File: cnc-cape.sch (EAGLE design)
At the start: 120 parts, among them IC1 LM2576hvt, IC2 74HC14N, IC3 74HC14N, IC4 74HCT244N, IC5 74HCT244N, IC6 74HC14N, IC7 LM1458N, J1 22-27-2041-04, J10 22-27-2031-03, J11 22-27-2031-03, J12 22-27-2031-03, J13 22-27-2031-03, J14 22-27-2031-03, J15 22-27-2031-03, J16 22-27-2031-03, J17 22-27-2031-03, J18 22-27-2031-03, J19 22-27-2031-03, J2 22-27-2041-04, J20 22-27-2031-03, J21 22-27-2031-03, J22 22-27-2031-03, J3 22-27-2041-04, J4 22-27-2041-04, J5 22-27-2041-04, J6 22-27-2031-03, J7 22-27-2031-03, J8 22-27-2031-03, J9 22-27-2031-03, K1 G2R2, K2 G2R2, K3 G2R2, Q1 2N7000, Q2 2N7000, T1 1n2222, T2 1n2222, T3 1n2222, X5 Power In

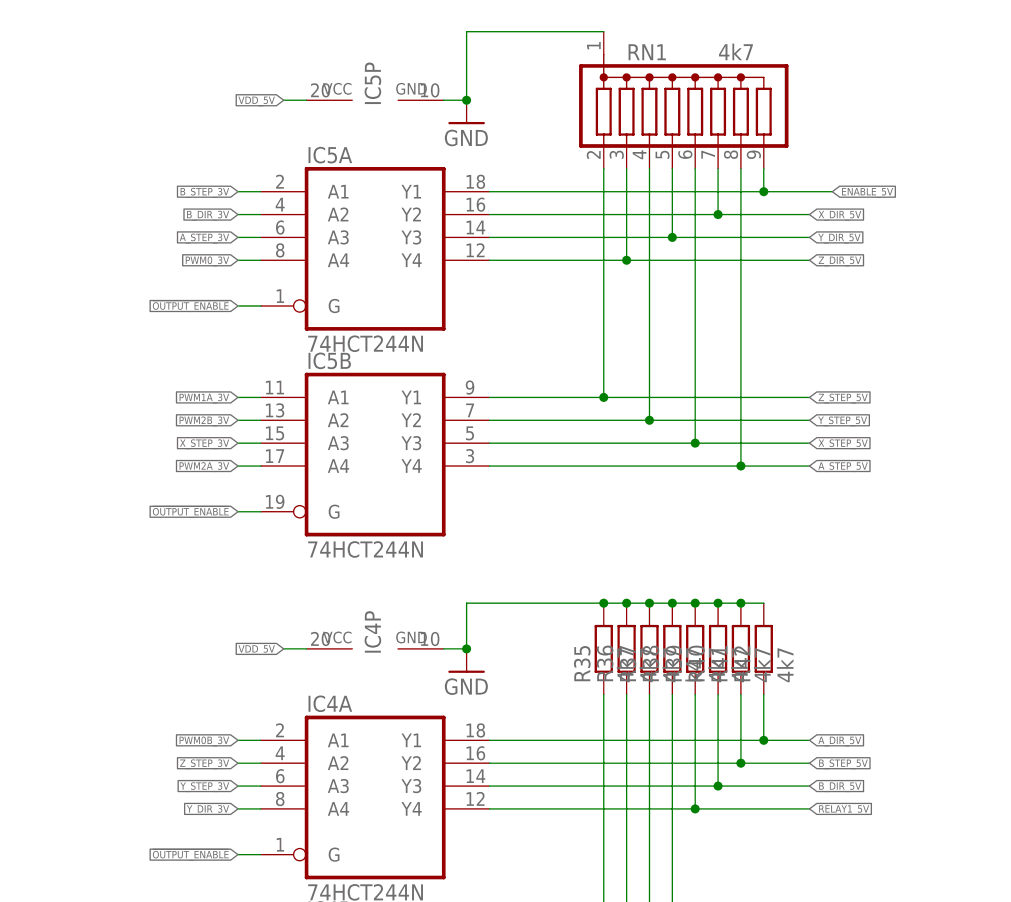
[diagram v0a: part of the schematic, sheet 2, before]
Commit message: Rearraged layout to reduce via count
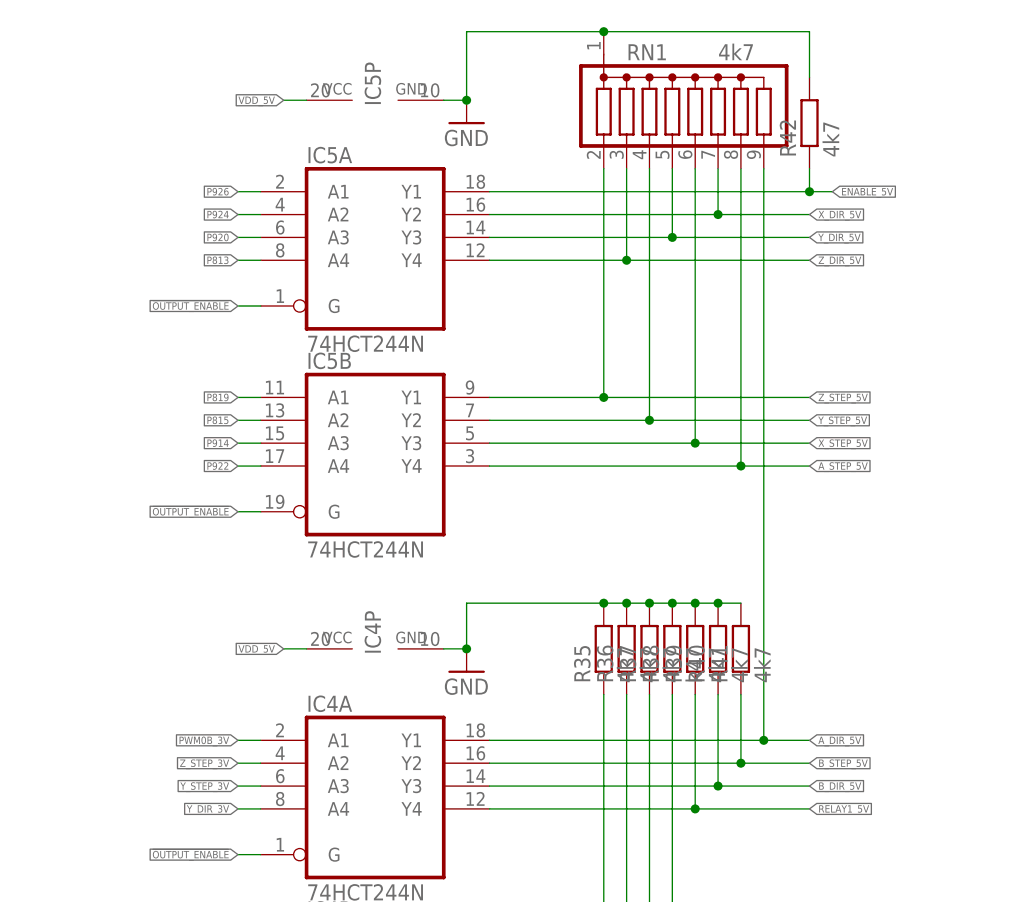
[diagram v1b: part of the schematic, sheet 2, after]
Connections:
- net B_DIR_3V renamed P924
- net B_STEP_3V renamed P926
- removed net A_STEP_3V: IC5A.A3, U$1.UART2_RXD
- removed net PWM0_3V: IC5A.A4, U$1.I2C2_SDA
- removed net PWM1A_3V: IC5B.A1, U$1.EHRPWM1A
- removed net PWM2A_3V: IC5B.A4, U$1.EHRPWM2A
- removed net PWM2B_3V: IC5B.A2, U$1.EHRPWM2B
- removed net X_STEP_3V: IC5B.A3, U$1.GPIO1_15
- new net P813: IC5A.A4, U$1.EHRPWM2B
- new net P815: IC5B.A2, U$1.GPIO1_15
- new net P819: IC5B.A1, U$1.EHRPWM2A
- new net P914: IC5B.A3, U$1.EHRPWM1A
- new net P920: IC5A.A3, U$1.I2C2_SDA
- new net P922: IC5B.A4, U$1.UART2_RXD
- net A_DIR_5V: now also RN1.9; no longer R42.1
- net ENABLE_5V: now also R42.1; no longer RN1.9
- net ENCODER0_A: now also IC2B.I, J7-2.S, LED2.C; no longer IC2C.I, J6-2.S, LED1.C
- net ENCODER0_B: now also IC2A.I, J8-2.S, LED3.C; no longer IC2B.I, J7-2.S, LED2.C
- net ENCODER0_I: now also IC2C.I, J6-2.S, LED1.C; no longer IC2A.I, J8-2.S, LED3.C
- net EQEP0A: now also IC2B.O; no longer IC2C.O
- net EQEP0B: now also IC2A.O; no longer IC2B.O
- net EQEP0I: now also IC2C.O; no longer IC2A.O
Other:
- moved on the sheet: R42

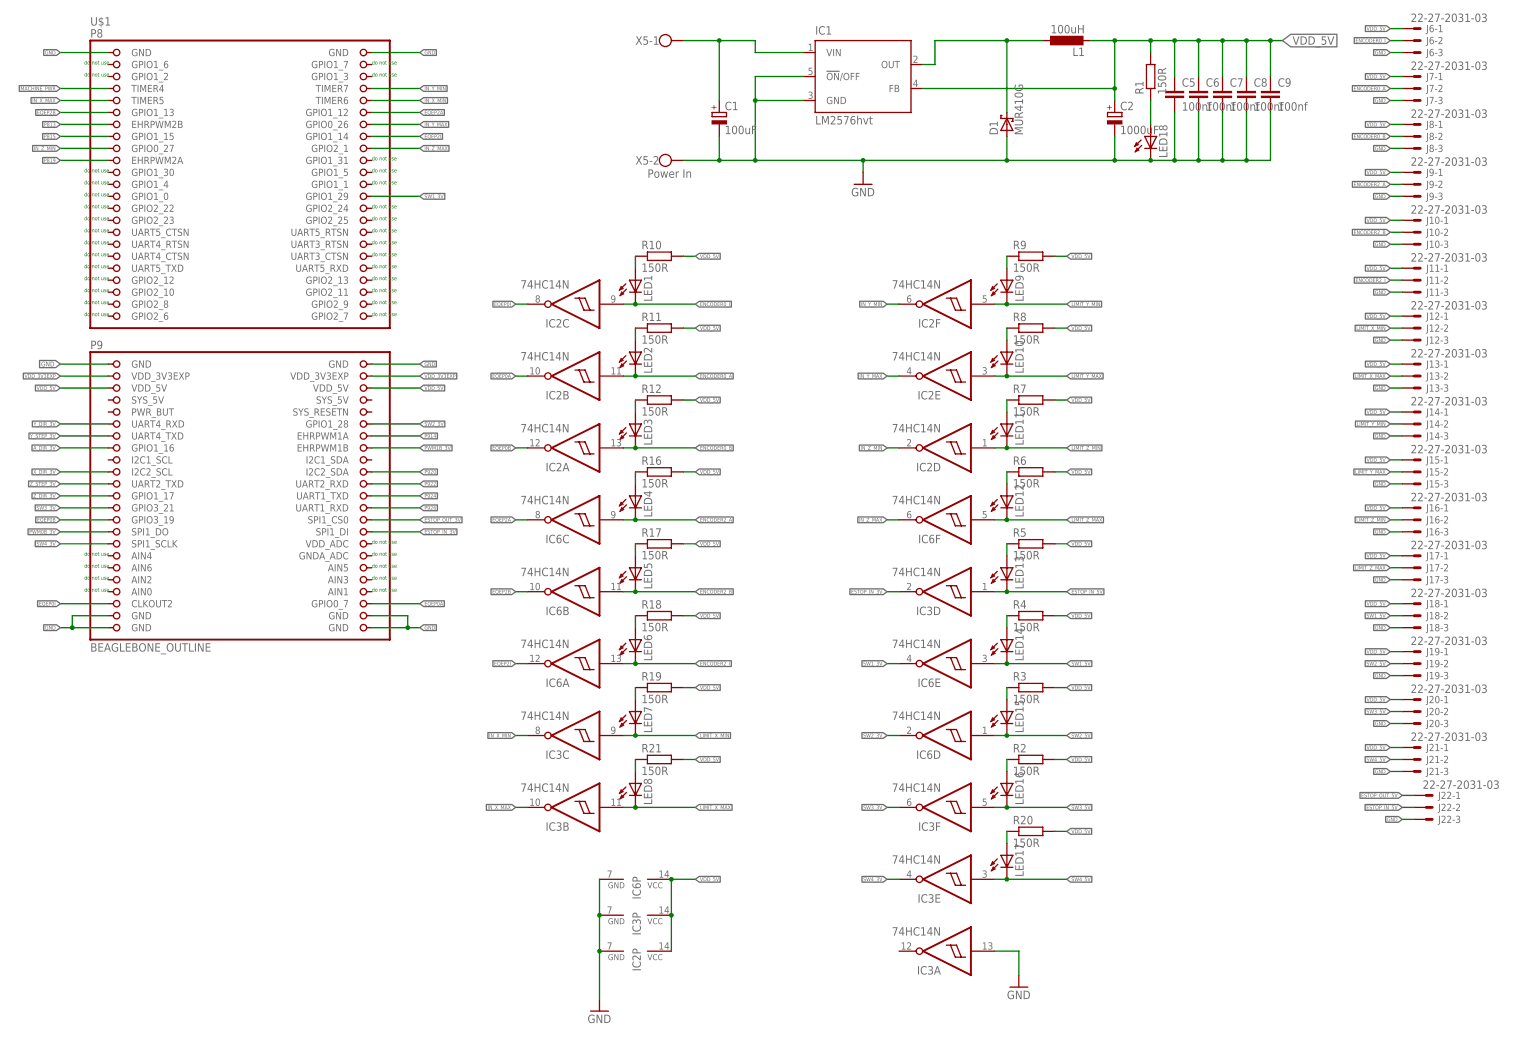
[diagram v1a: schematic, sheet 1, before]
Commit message: Fixed pwm polarity
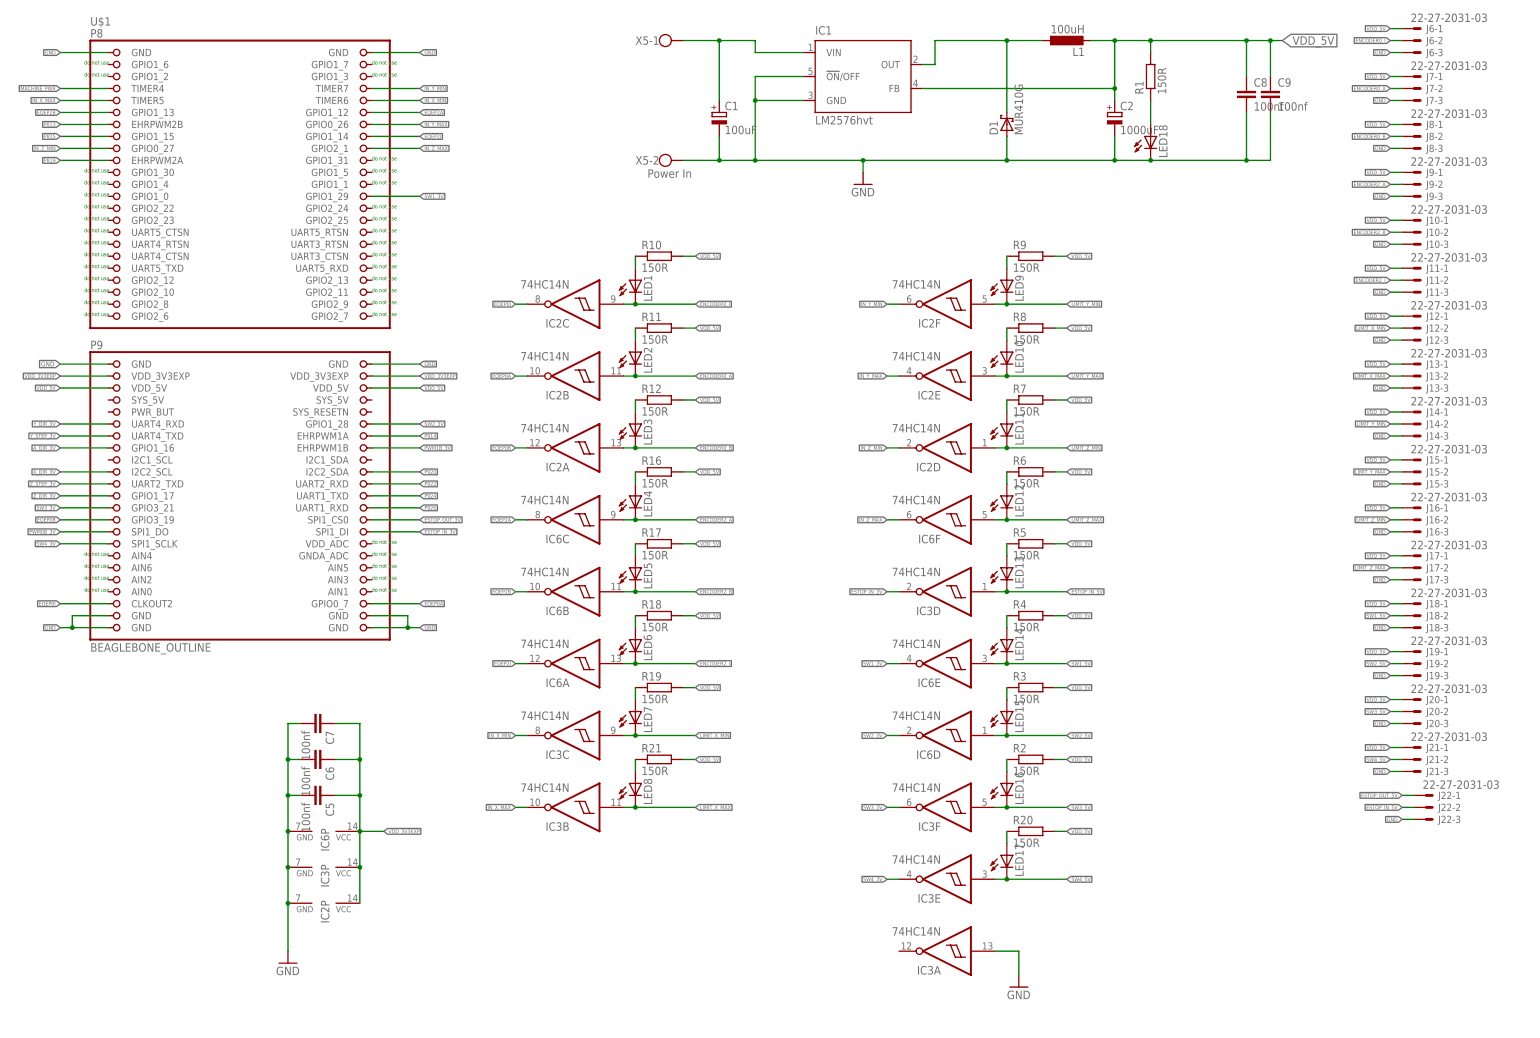
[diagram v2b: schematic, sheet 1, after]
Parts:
- R38: value k47 -> 4k7
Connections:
- net GND: no longer OK1.C
- net N$14: now also R31.2
- net N$45: now also OK1.C; no longer OK1.A
- net N$49: now also R31.1; no longer R31.2
- net SPINDLE-: no longer R31.1
- net VDD_3V3EXP: now also C5.1, C6.1, C7.1, IC2P.VCC, IC3P.VCC, IC6P.VCC
- net VDD_5V: now also OK1.A; no longer C5.1, C6.1, C7.1, IC2P.VCC, IC3P.VCC, IC6P.VCC
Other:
- moved on the sheet: C5, C6, C7, IC2P, IC3P, IC6P, R23, R31

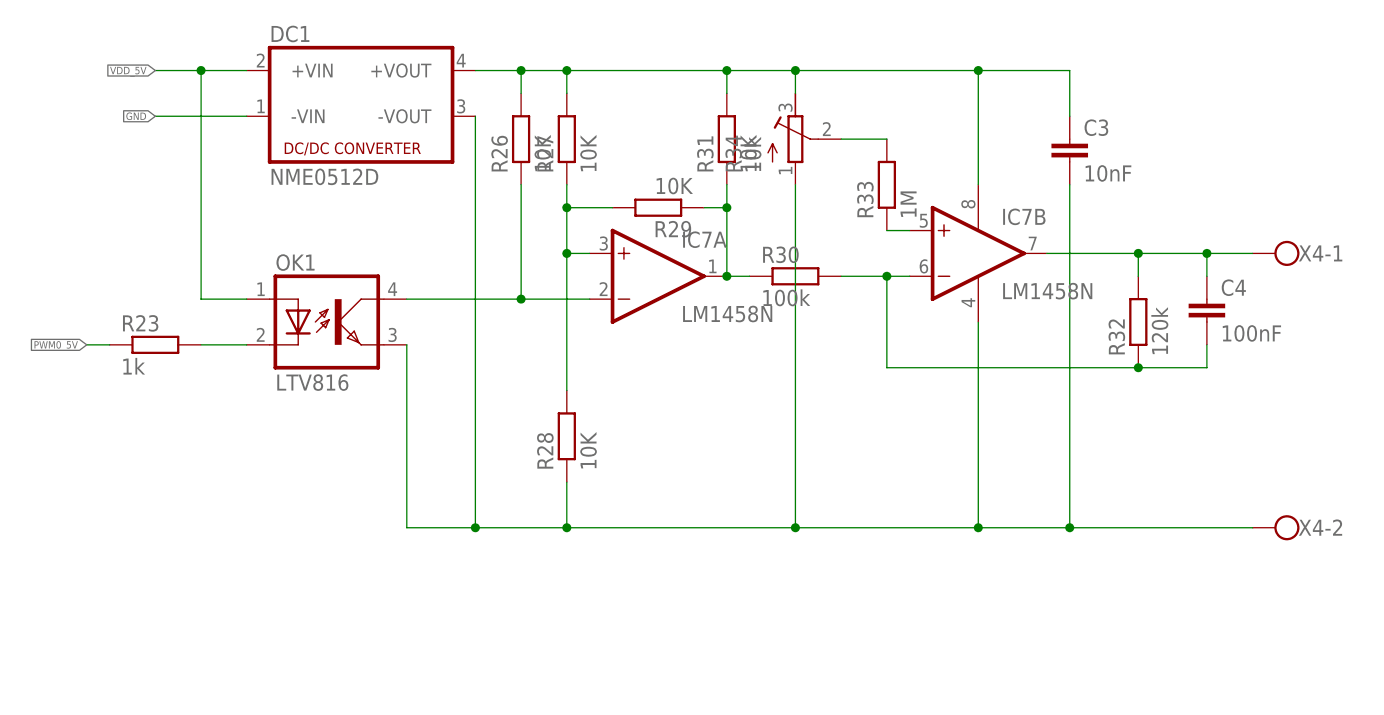
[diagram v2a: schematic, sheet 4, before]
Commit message: Added opto coupled inhibit out put, to disable spindle driver
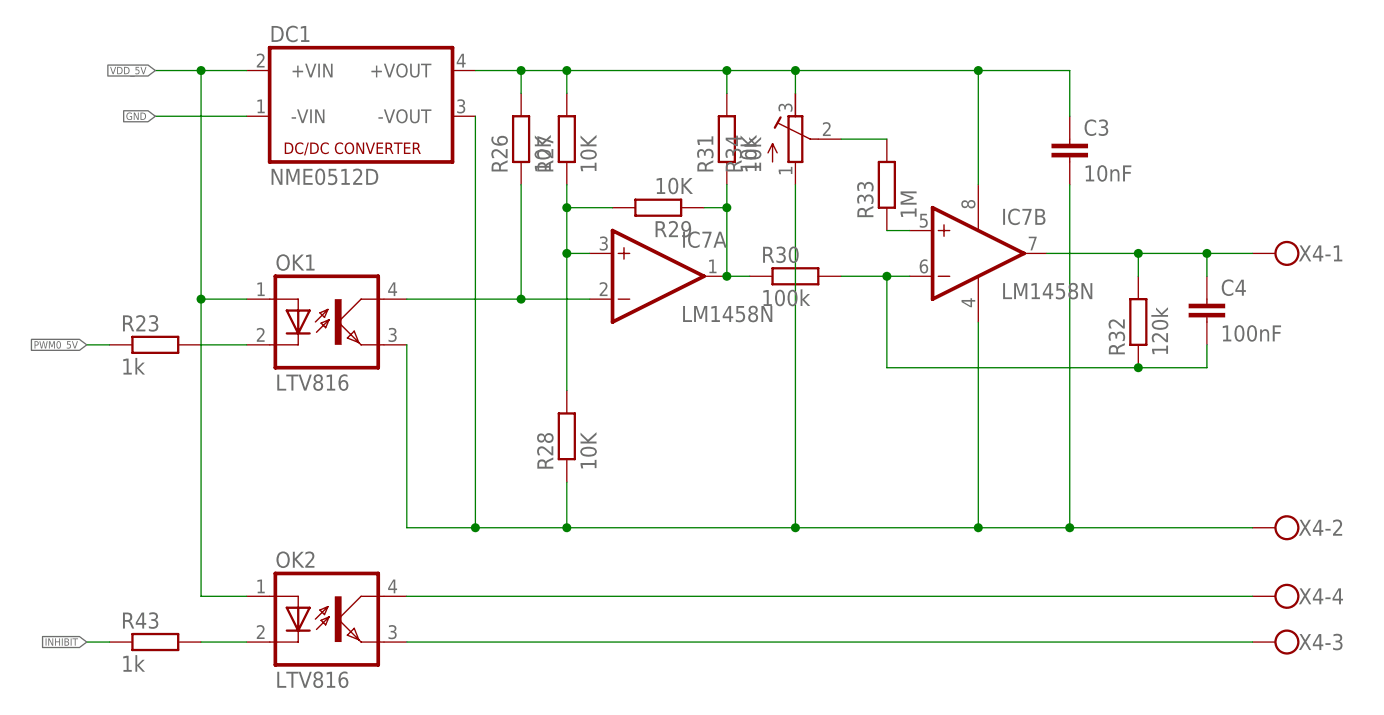
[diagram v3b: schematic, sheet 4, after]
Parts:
- added OK2: LTV816, optocoupler:LTV816
- added R43: 1k, rcl:R-EU_0204/5
- X4: device con-wago-500:W237-102 -> con-wago-500:W237-4
- X5: FARNELL (none) -> 3089034
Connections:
- removed net RELAY5_5V: IC4B.Y4, R35.1
- new net INHIBIT: IC4B.Y4, R35.1, R43.1
- new net N$46: OK2.COL, X4-4.KL
- new net N$51: OK2.EMIT, X4-3.KL
- new net N$52: OK2.C, R43.2
- net VDD_5V: now also OK2.A
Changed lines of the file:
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@@
 <part name="GND2" library="supply1" deviceset="GND" device=""/>
 <part name="GND3" library="supply1" deviceset="GND" device=""/>
-<part name="X4" library="con-wago-500" deviceset="W237-102" device=""/>
-<part name="X5" library="con-wago-500" deviceset="W237-102" device="" value="Power In"/>
+<part name="X4" library="con-wago-500" deviceset="W237-4" device=""/>
+<part name="X5" library="con-wago-500" deviceset="W237-102" device="" value="Power In">
+<attribute name="FARNELL" value="3089034"/>
+</part>
 <part name="LED18" library="led" deviceset="LED" device="3MM">
 <attribute name="FARNELL" value="1581133"/>
@@
 <part name="R41" library="rcl" deviceset="R-EU_" device="0204/5" value="4k7"/>
 <part name="R42" library="rcl" deviceset="R-EU_" device="0204/5" value="4k7"/>
+<part name="OK2" library="optocoupler" deviceset="LTV816" device=""/>
+<part name="R43" library="rcl" deviceset="R-EU_" device="0204/5" value="1k"/>
 </parts>
 <sheets>
@@
 <instance part="GND2" gate="1" x="-93.98" y="-68.58"/>
 <instance part="GND3" gate="1" x="60.96" y="-73.66"/>
-<instance part="X5" gate="-1" x="-15.24" y="127"/>
+<instance part="X5" gate="-1" x="-15.24" y="127">
+<attribute name="FARNELL" x="-15.24" y="127" size="1.778" layer="96" display="off"/>
+</instance>
 <instance part="X5" gate="-2" x="-15.24" y="101.6"/>
 <instance part="LED18" gate="G$1" x="88.9" y="106.68">
@@
 </segment>
 </net>
-<net name="RELAY5_5V" class="0">
+<net name="INHIBIT" class="0">
 <segment>
 <pinref part="IC4" gate="B" pin="Y4"/>
@@
 <wire x1="-33.02" y1="63.5" x2="-33.02" y2="27.94" width="0.1524" layer="91"/>
 <pinref part="R35" gate="G$1" pin="1"/>
+<wire x1="-33.02" y1="27.94" x2="-10.16" y2="27.94" width="0.1524" layer="91"/>
+<junction x="-33.02" y="27.94"/>
+<label x="-10.16" y="27.94" size="0.8128" layer="95" xref="yes"/>
 </segment>
 </net>
@@
 <instance part="X4" gate="-1" x="104.14" y="68.58" rot="R180"/>
 <instance part="X4" gate="-2" x="104.14" y="38.1" rot="R180"/>
+<instance part="X4" gate="-3" x="104.14" y="25.4" rot="R180"/>
+<instance part="X4" gate="-4" x="104.14" y="30.48" rot="R180"/>
+<instance part="OK2" gate="G$1" x="-2.54" y="27.94"/>
+<instance part="R43" gate="G$1" x="-22.86" y="25.4"/>
 </instances>
 <busses>
@@
 <wire x1="-17.78" y1="63.5" x2="-17.78" y2="88.9" width="0.1524" layer="91"/>
 <junction x="-17.78" y="88.9"/>
+<pinref part="OK2" gate="G$1" pin="A"/>
+<wire x1="-12.7" y1="30.48" x2="-17.78" y2="30.48" width="0.1524" layer="91"/>
+<wire x1="-17.78" y1="30.48" x2="-17.78" y2="63.5" width="0.1524" layer="91"/>
+<junction x="-17.78" y="63.5"/>
 </segment>
 </net>
@@
 </segment>
 </net>
+<net name="N$52" class="0">
+<segment>
+<pinref part="R43" gate="G$1" pin="2"/>
+<pinref part="OK2" gate="G$1" pin="C"/>
+<wire x1="-17.78" y1="25.4" x2="-12.7" y2="25.4" width="0.1524" layer="91"/>
+</segment>
+</net>
+<net name="INHIBIT" class="0">
+<segment>
+<pinref part="R43" gate="G$1" pin="1"/>
+<wire x1="-27.94" y1="25.4" x2="-30.48" y2="25.4" width="0.1524" layer="91"/>
+<label x="-30.48" y="25.4" size="0.8128" layer="95" rot="R180" xref="yes"/>
+</segment>
+</net>
+<net name="N$46" class="0">
+<segment>
+<pinref part="OK2" gate="G$1" pin="COL"/>
+<pinref part="X4" gate="-4" pin="KL"/>
+<wire x1="5.08" y1="30.48" x2="99.06" y2="30.48" width="0.1524" layer="91"/>
+</segment>
+</net>
+<net name="N$51" class="0">
+<segment>
+<pinref part="OK2" gate="G$1" pin="EMIT"/>
+<pinref part="X4" gate="-3" pin="KL"/>
+<wire x1="5.08" y1="25.4" x2="99.06" y2="25.4" width="0.1524" layer="91"/>
+</segment>
+</net>
